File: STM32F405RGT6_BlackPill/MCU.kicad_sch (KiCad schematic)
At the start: 39 parts, among them J100 Conn_01x04, J101 Conn_02x15_Odd_Even, J102 Conn_02x10_Odd_Even, U100 STM32F405RGTx, Y1 32768Hz, Y100 25Mhz

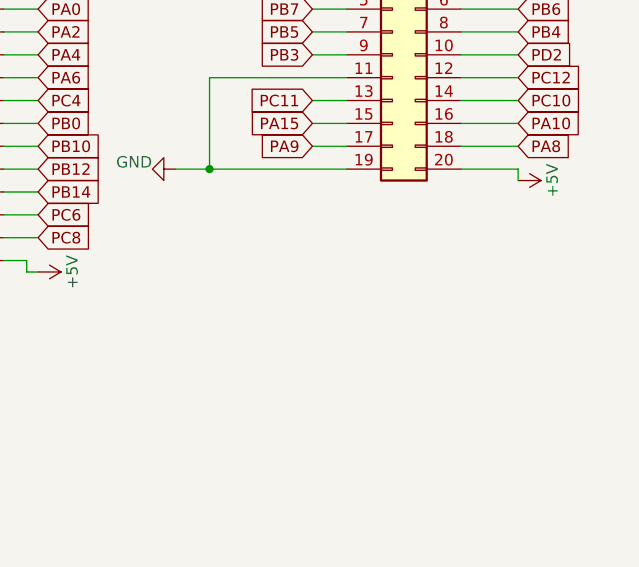
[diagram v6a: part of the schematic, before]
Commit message: VBUS | GND connector, manufacture files
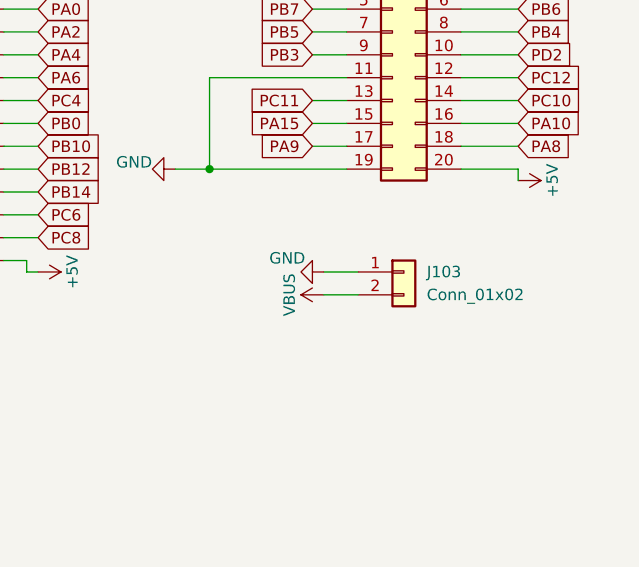
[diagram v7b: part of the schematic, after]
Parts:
- added J103: Conn_01x02, Connector_PinHeader_2.54mm:PinHeader_1x02_P2.54mm_Vertical, symbol Connector_Generic:Conn_01x02
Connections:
- net GND: now also J103.1 (Pin_1)
- new net VBUS: J103.2 (Pin_2)
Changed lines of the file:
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@@
 	(wire
 		(pts
+			(xy 236.22 120.65) (xy 240.03 120.65)
+		)
+		(stroke
+			(width 0)
+			(type default)
+		)
+	)
+	(wire
+		(pts
 			(xy 105.41 44.45) (xy 101.6 44.45)
 		)
@@
 	(wire
 		(pts
+			(xy 236.22 118.11) (xy 240.03 118.11)
+		)
+		(stroke
+			(width 0)
+			(type default)
+		)
+	)
+	(wire
+		(pts
 			(xy 45.72 76.2) (xy 45.72 82.55)
 		)
@@
 	(symbol
 		(lib_id "power:GND")
+		(at 236.22 118.11 270)
+		(unit 1)
+		(exclude_from_sim no)
+		(in_bom yes)
+		(on_board yes)
+		(dnp no)
+		(property "Reference" "#PWR045"
+			(at 229.87 118.11 0)
+			(effects
+				(font
+					(size 1.27 1.27)
+				)
+				(hide yes)
+			)
+		)
+		(property "Value" "GND"
+			(at 232.156 116.586 90)
+			(effects
+				(font
+					(size 1.27 1.27)
+				)
+			)
+		)
+		(property "Footprint" ""
+			(at 236.22 118.11 0)
+			(effects
+				(font
+					(size 1.27 1.27)
+				)
+				(hide yes)
+			)
+		)
+		(property "Datasheet" ""
+			(at 236.22 118.11 0)
+			(effects
+				(font
+					(size 1.27 1.27)
+				)
+				(hide yes)
+			)
+		)
+		(property "Description" "Power symbol creates a global label with name \"GND\" , ground"
+			(at 236.22 118.11 0)
+			(effects
+				(font
+					(size 1.27 1.27)
+				)
+				(hide yes)
+			)
+		)
+		(pin "1"
+		)
+		(instances
+			(project "STM32F405RGT6_BlackPill"
+				(path "/cae5b0ba-cc42-4347-bdfb-a704c1b808ff/dd7f6eda-dc83-4b84-a9a2-d4778c0007f8"
+					(reference "#PWR045")
+					(unit 1)
+				)
+			)
+		)
+	)
+	(symbol
+		(lib_id "power:GND")
 		(at 242.57 44.45 0)
 		(unit 1)
@@
 	)
 	(symbol
+		(lib_name "BlackPillLibrary:SW_PUSH_6mm_H5mm")
 		(lib_id "BlackPillLibrary:SW_PUSH_6mm_H5mm")
 		(at 29.21 119.38 270)
@@
 	)
 	(symbol
+		(lib_id "power:VBUS")
+		(at 236.22 120.65 90)
+		(unit 1)
+		(exclude_from_sim no)
+		(in_bom yes)
+		(on_board yes)
+		(dnp no)
+		(property "Reference" "#PWR049"
+			(at 240.03 120.65 0)
+			(effects
+				(font
+					(size 1.27 1.27)
+				)
+				(hide yes)
+			)
+		)
+		(property "Value" "VBUS"
+			(at 232.41 120.65 0)
+			(effects
+				(font
+					(size 1.27 1.27)
+				)
+			)
+		)
+		(property "Footprint" ""
+			(at 236.22 120.65 0)
+			(effects
+				(font
+					(size 1.27 1.27)
+				)
+				(hide yes)
+			)
+		)
+		(property "Datasheet" ""
+			(at 236.22 120.65 0)
+			(effects
+				(font
+					(size 1.27 1.27)
+				)
+				(hide yes)
+			)
+		)
+		(property "Description" ""
+			(at 236.22 120.65 0)
+			(effects
+				(font
+					(size 1.27 1.27)
+				)
+				(hide yes)
+			)
+		)
+		(pin "1"
+		)
+		(instances
+			(project "STM32F405RGT6_BlackPill"
+				(path "/cae5b0ba-cc42-4347-bdfb-a704c1b808ff/dd7f6eda-dc83-4b84-a9a2-d4778c0007f8"
+					(reference "#PWR049")
+					(unit 1)
+				)
+			)
+		)
+	)
+	(symbol
 		(lib_id "power:+3.3V")
 		(at 20.32 22.86 0)
@@
 	)
 	(symbol
+		(lib_name "BlackPillLibrary:SW_PUSH_6mm_H5mm")
 		(lib_id "BlackPillLibrary:SW_PUSH_6mm_H5mm")
 		(at 96.52 35.56 270)
@@
 	)
 	(symbol
+		(lib_id "Connector_Generic:Conn_01x02")
+		(at 245.11 118.11 0)
+		(unit 1)
+		(exclude_from_sim no)
+		(in_bom yes)
+		(on_board yes)
+		(dnp no)
+		(fields_autoplaced yes)
+		(property "Reference" "J103"
+			(at 247.65 118.1099 0)
+			(effects
+				(font
+					(size 1.27 1.27)
+				)
+				(justify left)
+			)
+		)
+		(property "Value" "Conn_01x02"
+			(at 247.65 120.6499 0)
+			(effects
+				(font
+					(size 1.27 1.27)
+				)
+				(justify left)
+			)
+		)
+		(property "Footprint" "Connector_PinHeader_2.54mm:PinHeader_1x02_P2.54mm_Vertical"
+			(at 245.11 118.11 0)
+			(effects
+				(font
+					(size 1.27 1.27)
+				)
+				(hide yes)
+			)
+		)
+		(property "Datasheet" "~"
+			(at 245.11 118.11 0)
+			(effects
+				(font
+					(size 1.27 1.27)
+				)
+				(hide yes)
+			)
+		)
+		(property "Description" "Generic connector, single row, 01x02, script generated (kicad-library-utils/schlib/autogen/connector/)"
+			(at 245.11 118.11 0)
+			(effects
+				(font
+					(size 1.27 1.27)
+				)
+				(hide yes)
+			)
+		)
+		(pin "2"
+		)
+		(pin "1"
+		)
+		(instances
+			(project ""
+				(path "/cae5b0ba-cc42-4347-bdfb-a704c1b808ff/dd7f6eda-dc83-4b84-a9a2-d4778c0007f8"
+					(reference "J103")
+					(unit 1)
+				)
+			)
+		)
+	)
+	(symbol
 		(lib_id "power:GND")
 		(at 52.07 45.72 0)
@@
 	)
 	(symbol
+		(lib_name "BlackPillLibrary:SW_PUSH_6mm_H5mm")
 		(lib_id "BlackPillLibrary:SW_PUSH_6mm_H5mm")
 		(at 27.94 33.02 270)
